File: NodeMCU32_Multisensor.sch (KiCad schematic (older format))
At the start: 1 part, among them U1 ESP32-DEVKITC-32D

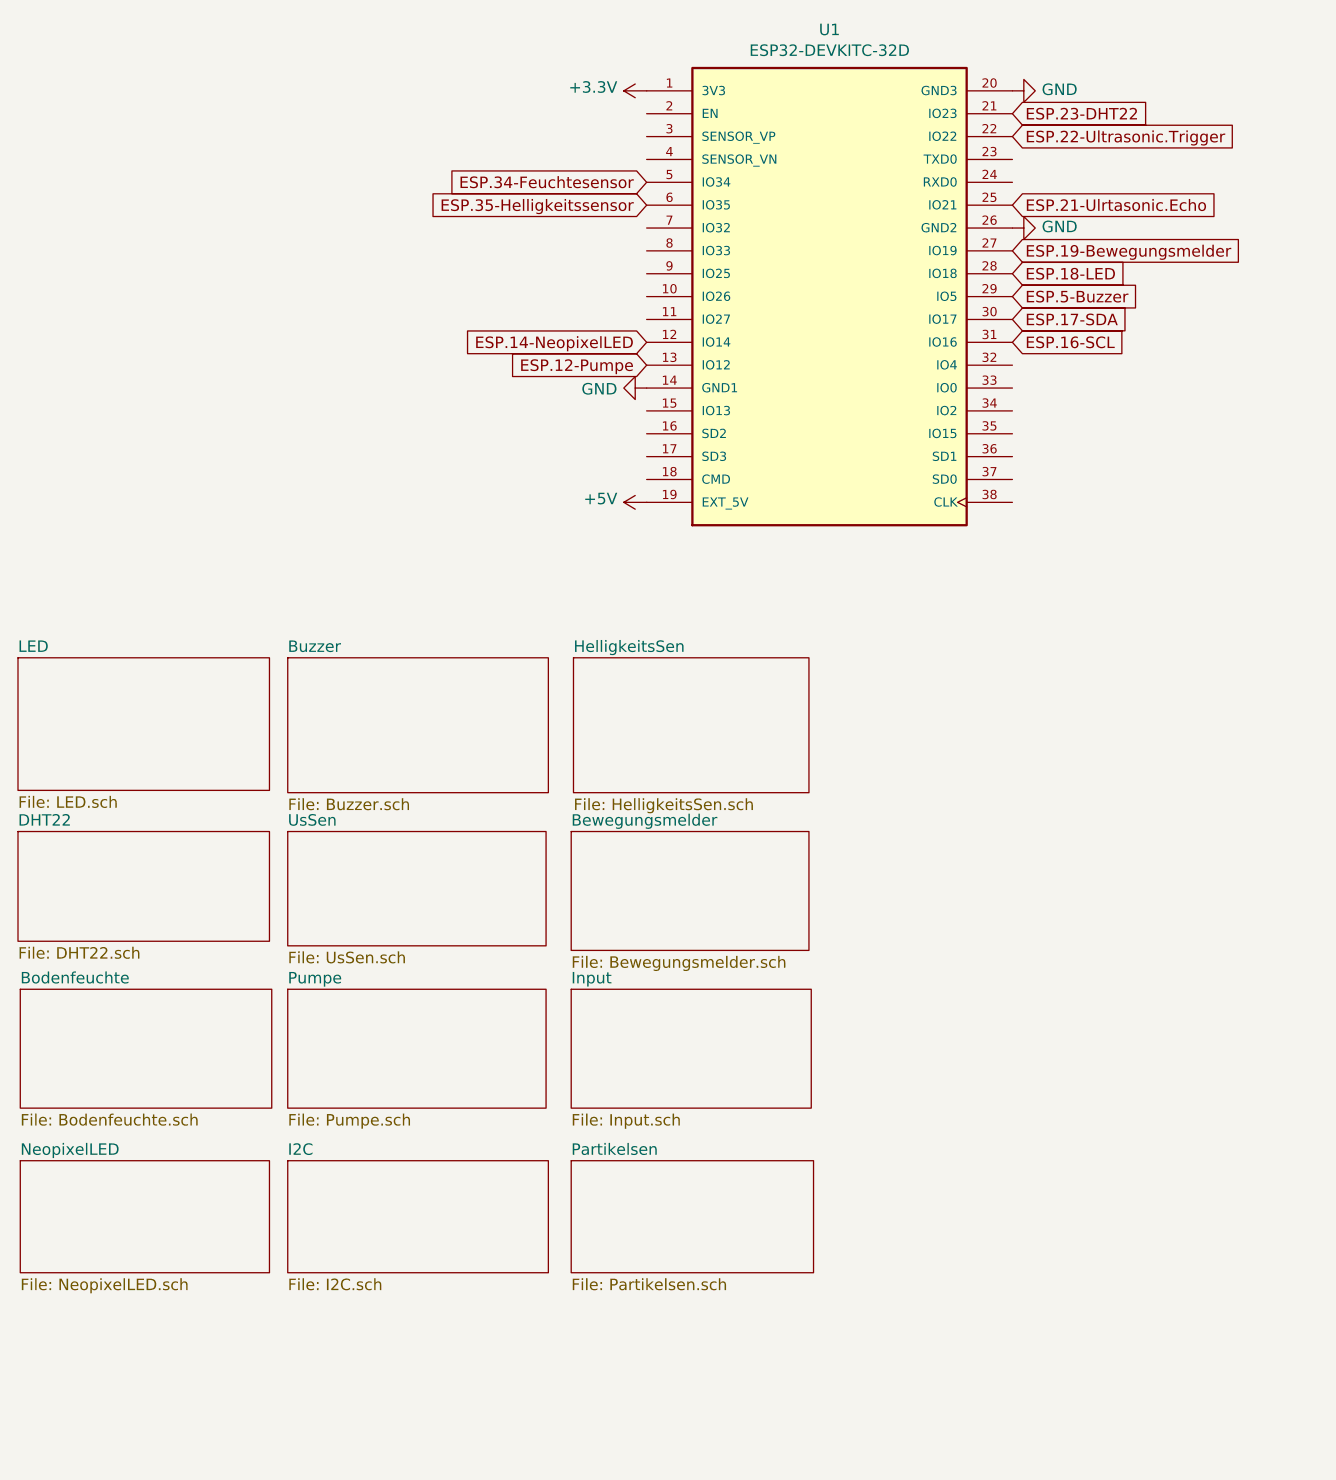
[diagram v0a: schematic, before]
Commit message: added sensors, finished schematics yet
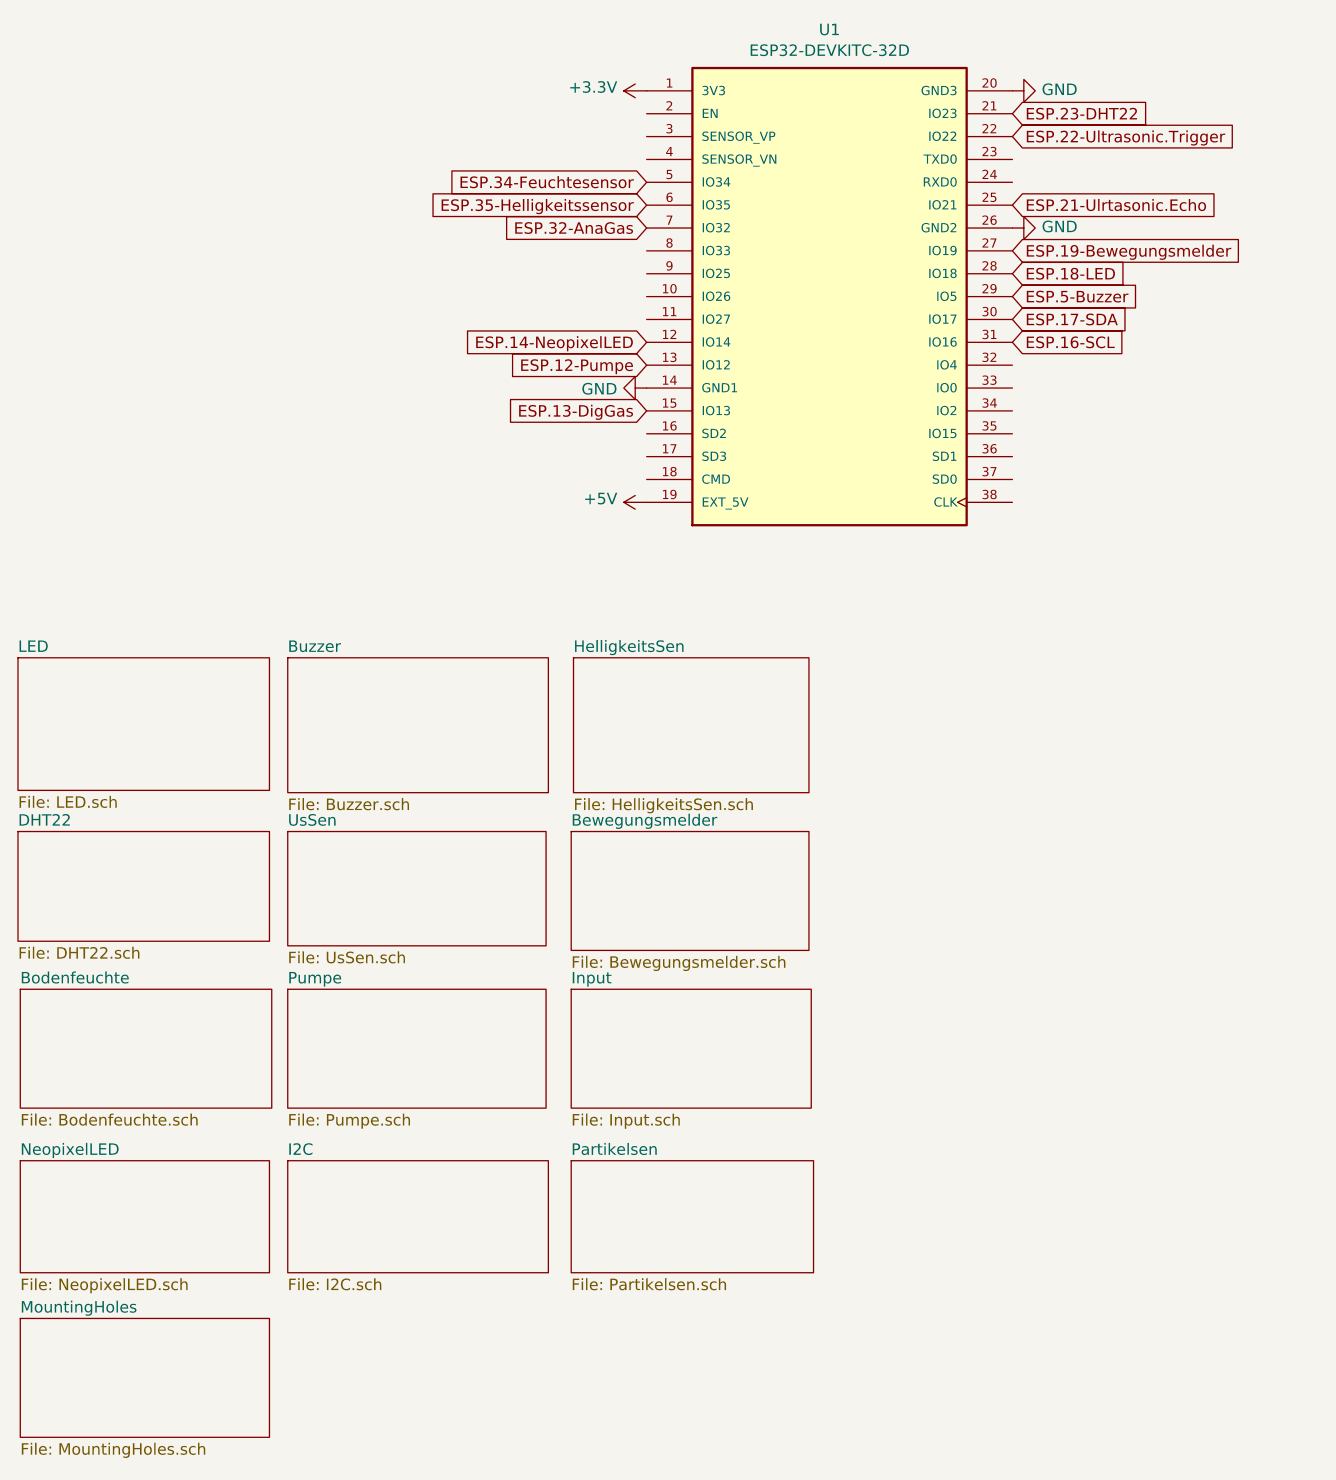
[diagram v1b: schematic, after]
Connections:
- net ESP.13-DigGas: now reaches U1.15 (IO13)
- net ESP.32-AnaGas: now reaches U1.7 (IO32)
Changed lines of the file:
@@
 $Descr A4 11693 8268
 encoding utf-8
-Sheet 1 13
+Sheet 1 14
 Title ""
 Date ""
@@
 F1 "Partikelsen.sch" 50
 $EndSheet
+Text GLabel 4050 2850 0    50   Input ~ 0
+ESP.13-DigGas
+Text GLabel 4050 2050 0    50   Input ~ 0
+ESP.32-AnaGas
+$Sheet
+S 1310 6820 1090 520
+U 60D5FAAB
+F0 "MountingHoles" 50
+F1 "MountingHoles.sch" 50
+$EndSheet
 $EndSCHEMATC
